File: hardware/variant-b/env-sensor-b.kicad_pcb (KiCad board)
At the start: 4 copper layers, 30 x 51 mm, 64 parts, among them J1 USB-C 16P, J2 Molex PicoBlade 3P, Q1 2N7002, SW1 SW_PROV, U1 ESP32-C6-MINI-1-N4, U2 SHT45-AD1F, U3 TPS62840DLC, U4 BQ24074RGTR, U5 USBLC6-2SC6

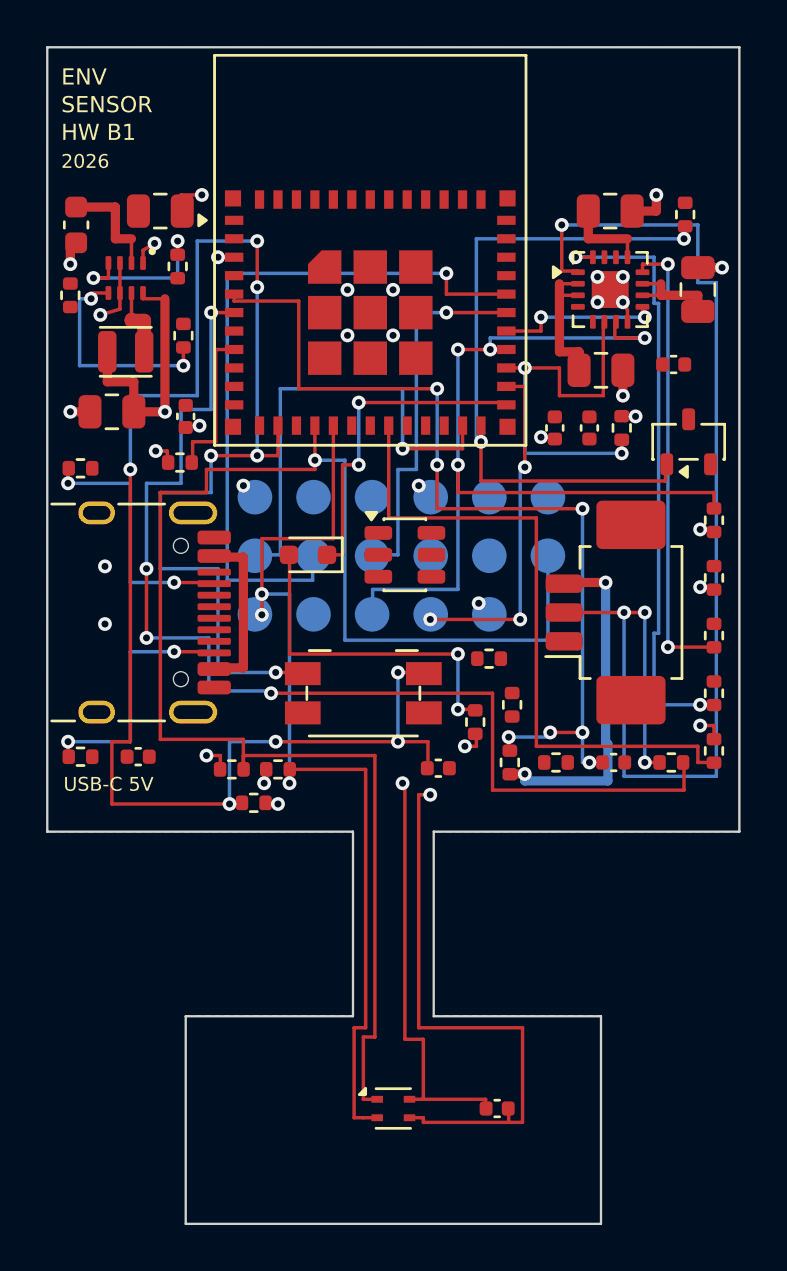
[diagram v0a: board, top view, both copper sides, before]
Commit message: build(boardgen): regenerate local charger programming layout
Regenerate both variants from the local C9/R12/R13 placement and routing correction. Fresh reports retain A42/B34 incomplete development connectivity and zero errors, warnings or parity differences; these generated boards are not fabrication approval.
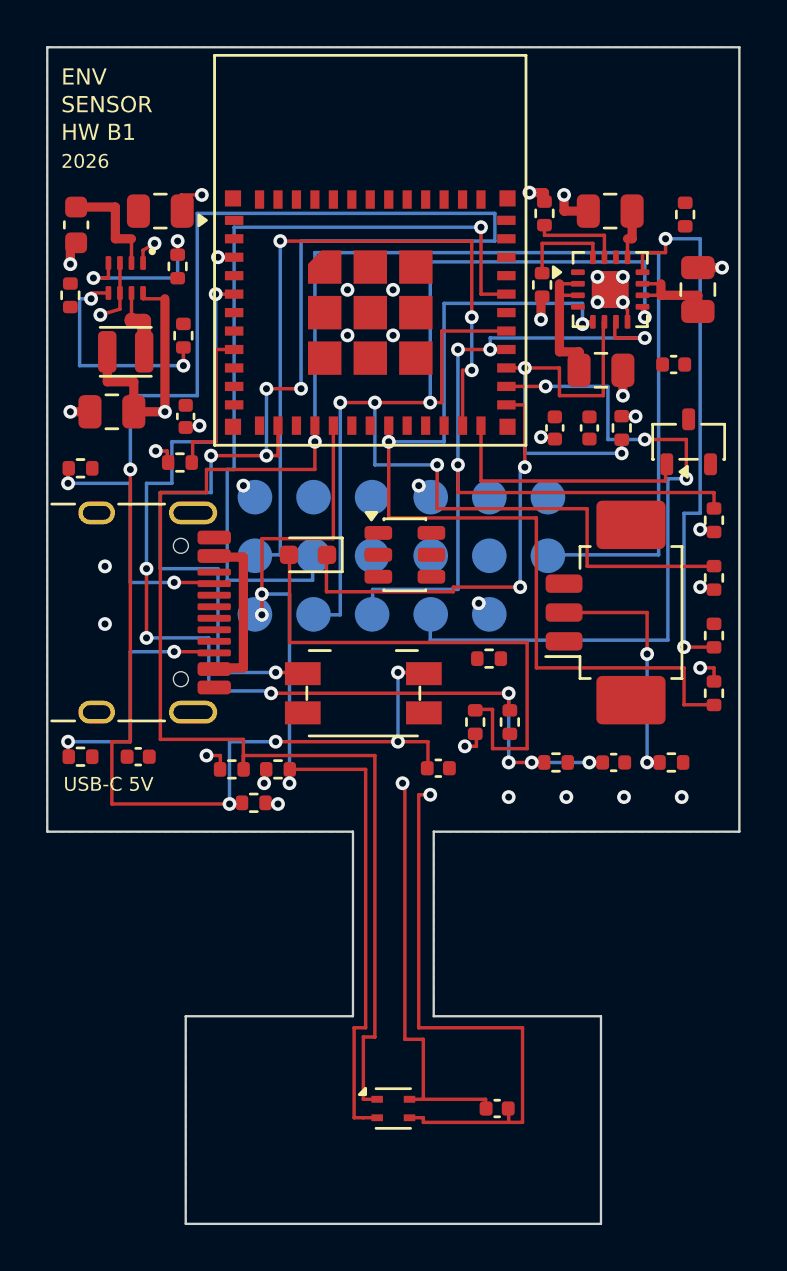
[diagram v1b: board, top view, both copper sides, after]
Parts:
- moved R12 19.4 mm to (121.5, 67.2), turned to 90 degrees
- moved R13 19.2 mm to (121.5, 70.3), turned to 270 degrees
- moved R20 2.50 mm to (128.9, 88.0)
- moved R18 2.24 mm to (119.2, 86.5), turned to 0 degrees
- moved R14 1.75 mm to (120.0, 89.2)
- turned C9 to 180 degrees
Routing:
- net CHG_N: track 7.20 -> 60.9 mm, vias 2 -> 5
- net PACK_TS_SENSE: track 49.0 -> 0.00 mm, vias 4 -> 0
- net PACK_TS: track 55.1 -> 10.6 mm, vias 4 -> 2
- net BTN_PROV: track 84.1 -> 106.7 mm
- net ISET: track 26.5 -> 4.09 mm, vias 2 -> 0
- net SDA: track 69.1 -> 88.5 mm
- net CHARGE_ENABLE: track 29.6 -> 11.1 mm, vias 2 -> 0
- net UART_RX: track 16.3 -> 0.00 mm, vias 1 -> 0
- net TEST_MODE: track 15.0 -> 31.0 mm
- net VBAT: track 21.3 -> 6.20 mm, vias 2 -> 0
- net USB_EN2: track 28.7 -> 42.0 mm, vias 0 -> 2
- net BOOT_N: track 19.8 -> 31.4 mm, vias 1 -> 3
- net LED_A: track 14.8 -> 22.6 mm, vias 2 -> 0
- net VBAT_SENSE: track 40.3 -> 45.1 mm, vias 7 -> 8
- net LED_N: track 14.5 -> 19.1 mm
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
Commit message: build(boardgen): regenerate plane-connected body ground regions
Regenerate both layouts after adding explicit U1/C5/J2/U5 ground access. Fresh reports show no GND airwires, no errors/warnings/parity differences and A39/B35 total unfinished connections. Record exact development counts; fabrication remains blocked.
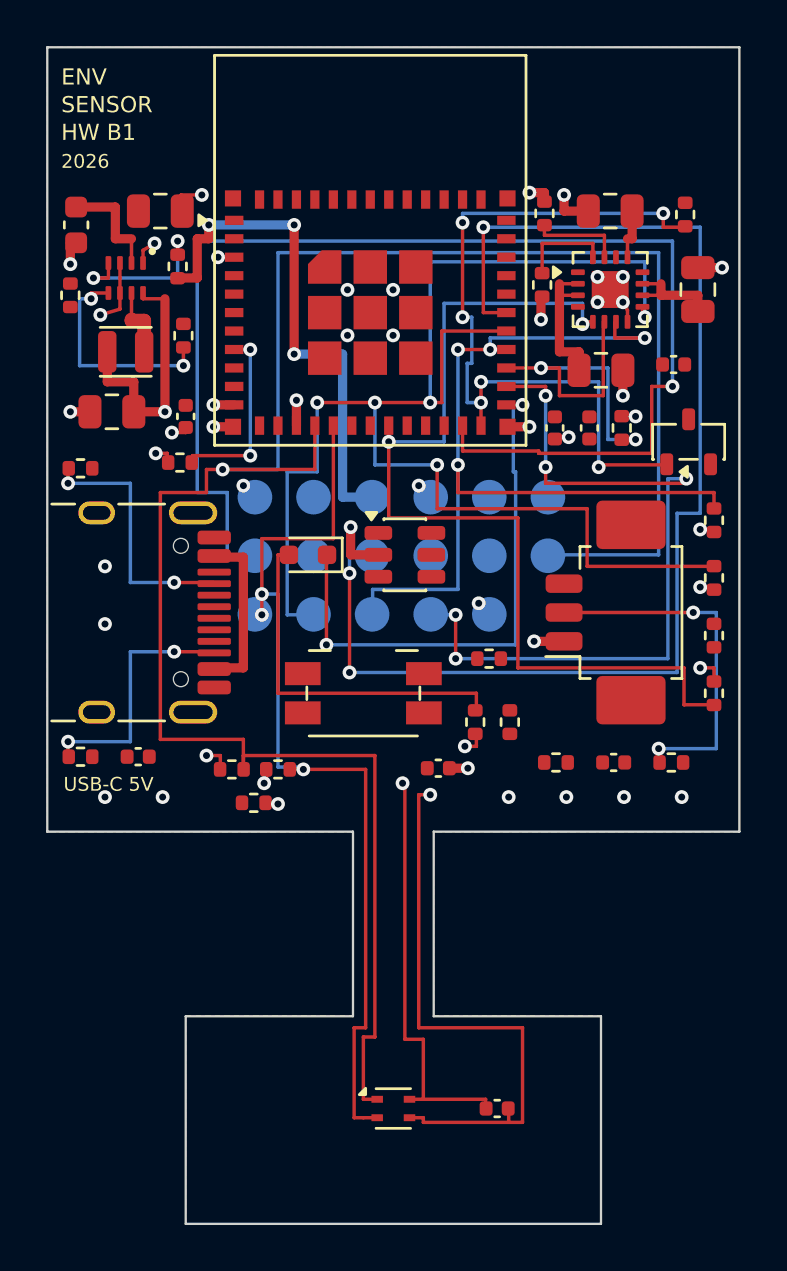
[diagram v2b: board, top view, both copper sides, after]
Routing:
- net BTN_PROV: track 106.7 -> 0.00 mm, vias 10 -> 0
- net UART_RX: track 0.00 -> 54.7 mm, vias 0 -> 3
- net VBAT_SENSE: track 45.1 -> 0.00 mm, vias 8 -> 0
- net UART_TX: track 35.1 -> 0.00 mm, vias 1 -> 0
- net BOOT_N: track 31.4 -> 56.2 mm, vias 3 -> 1
- net ILIM: track 23.7 -> 0.00 mm, vias 2 -> 0
- net VSYS: track 9.22 -> 31.8 mm, vias 0 -> 3
- net CHARGE_ENABLE: track 11.1 -> 33.3 mm, vias 0 -> 6
- net GND: track 33.2 -> 41.5 mm, vias 26 -> 35
- net LED_A: track 22.6 -> 15.8 mm
- net SDA: track 88.5 -> 93.7 mm
- net PACK_TS: track 10.6 -> 15.6 mm
- net LED_N: track 19.1 -> 23.7 mm
- net CHG_N: track 60.9 -> 63.1 mm
- net TEST_MODE: track 31.0 -> 33.0 mm, vias 3 -> 5
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
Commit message: build(boardgen): regenerate guarded USB layouts and fixture map
Regenerate both board layouts, design rules, fixture coordinates and mechanical placement inputs from the guarded USB generator. Fresh filled-board reports have zero errors, warnings and parity differences, with A31/B27 total unconnected items; neither USB data net nor GND has an airwire. Physical and fabrication qualification remain open.
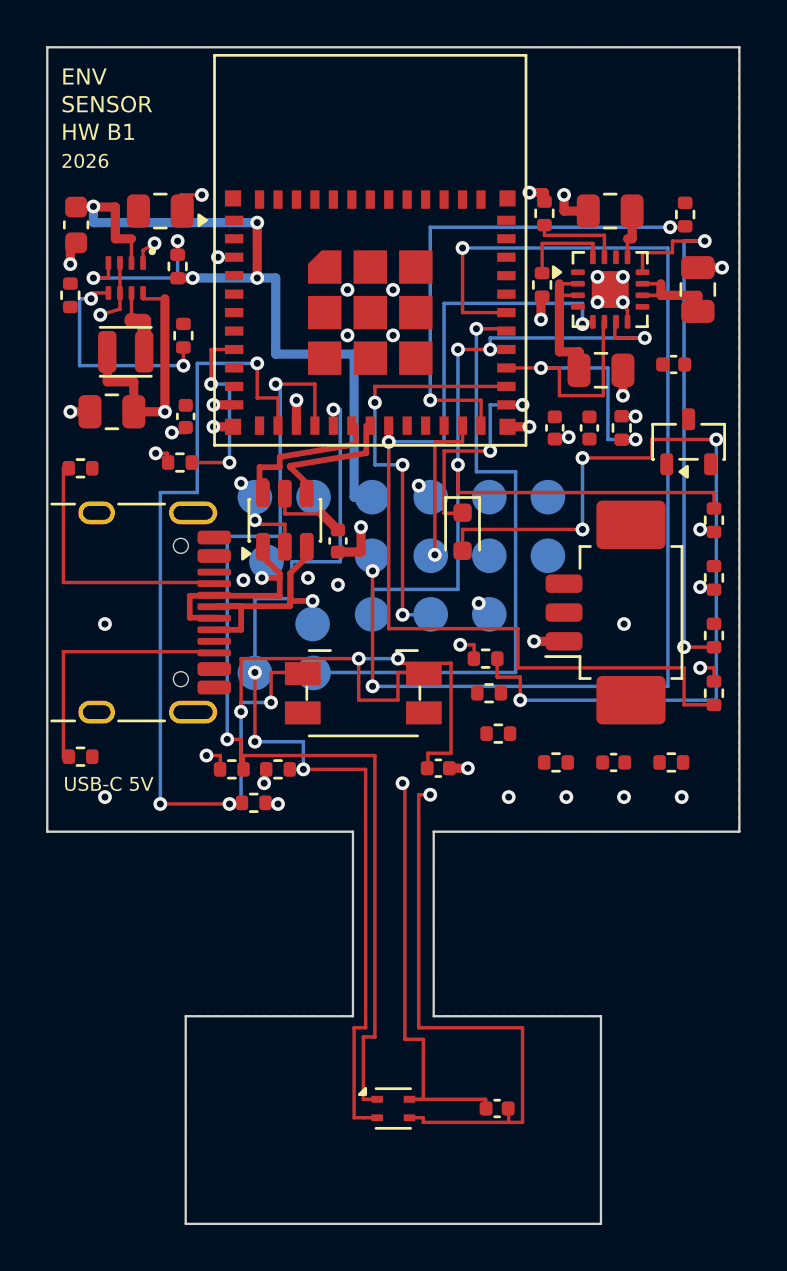
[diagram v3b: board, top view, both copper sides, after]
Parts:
- moved C14 12.7 mm to (112.6, 81.4), turned to 270 degrees
- moved TP11 9.66 mm to (109.5, 82.3)
- moved TP7 7.62 mm to (116.6, 82.0)
- moved TP8 7.62 mm to (119.2, 82.0)
- moved D1 6.77 mm to (118.0, 81.0), turned to 90 degrees
- moved TP10 5.91 mm to (111.5, 85.0)
- moved U5 5.41 mm to (110.3, 80.5), turned to 90 degrees
- moved R2 2.79 mm to (119.0, 86.5), turned to 0 degrees
- moved TP13 2.54 mm to (109.0, 87.1)
- moved TP14 2.54 mm to (111.5, 87.1)
- moved R18 1.50 mm to (119.2, 88.0)
- moved R14 0.71 mm to (119.5, 89.8), turned to 0 degrees
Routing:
- net BTN_PROV: track 0.00 -> 62.2 mm, vias 0 -> 7
- net BOOT_N: track 56.2 -> 6.80 mm
- net SDA: track 93.7 -> 45.7 mm, vias 1 -> 2
- net CHG_N: track 63.1 -> 26.8 mm, vias 5 -> 1
- net ILIM: track 0.00 -> 23.9 mm, vias 0 -> 2
- net LED_A: track 15.8 -> 38.4 mm, vias 0 -> 4
- net USB_D_P: track 0.00 -> 15.9 mm, vias 0 -> 1
- net USB_D_N: track 0.00 -> 15.7 mm, vias 0 -> 1
- net PACK_TS: track 15.6 -> 0.00 mm, vias 2 -> 0
- net TEST_MODE: track 33.0 -> 18.0 mm, vias 5 -> 3
- net LED_N: track 23.7 -> 9.60 mm
- net CHARGE_ENABLE: track 33.3 -> 21.8 mm, vias 6 -> 2
- net VSYS: track 31.8 -> 38.1 mm, vias 3 -> 4
- net VBUS: track 9.80 -> 5.67 mm
- net UART_RX: track 54.7 -> 51.1 mm
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- added copper zone on In2.Cu, net GND
